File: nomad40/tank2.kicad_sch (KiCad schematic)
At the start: 56 parts

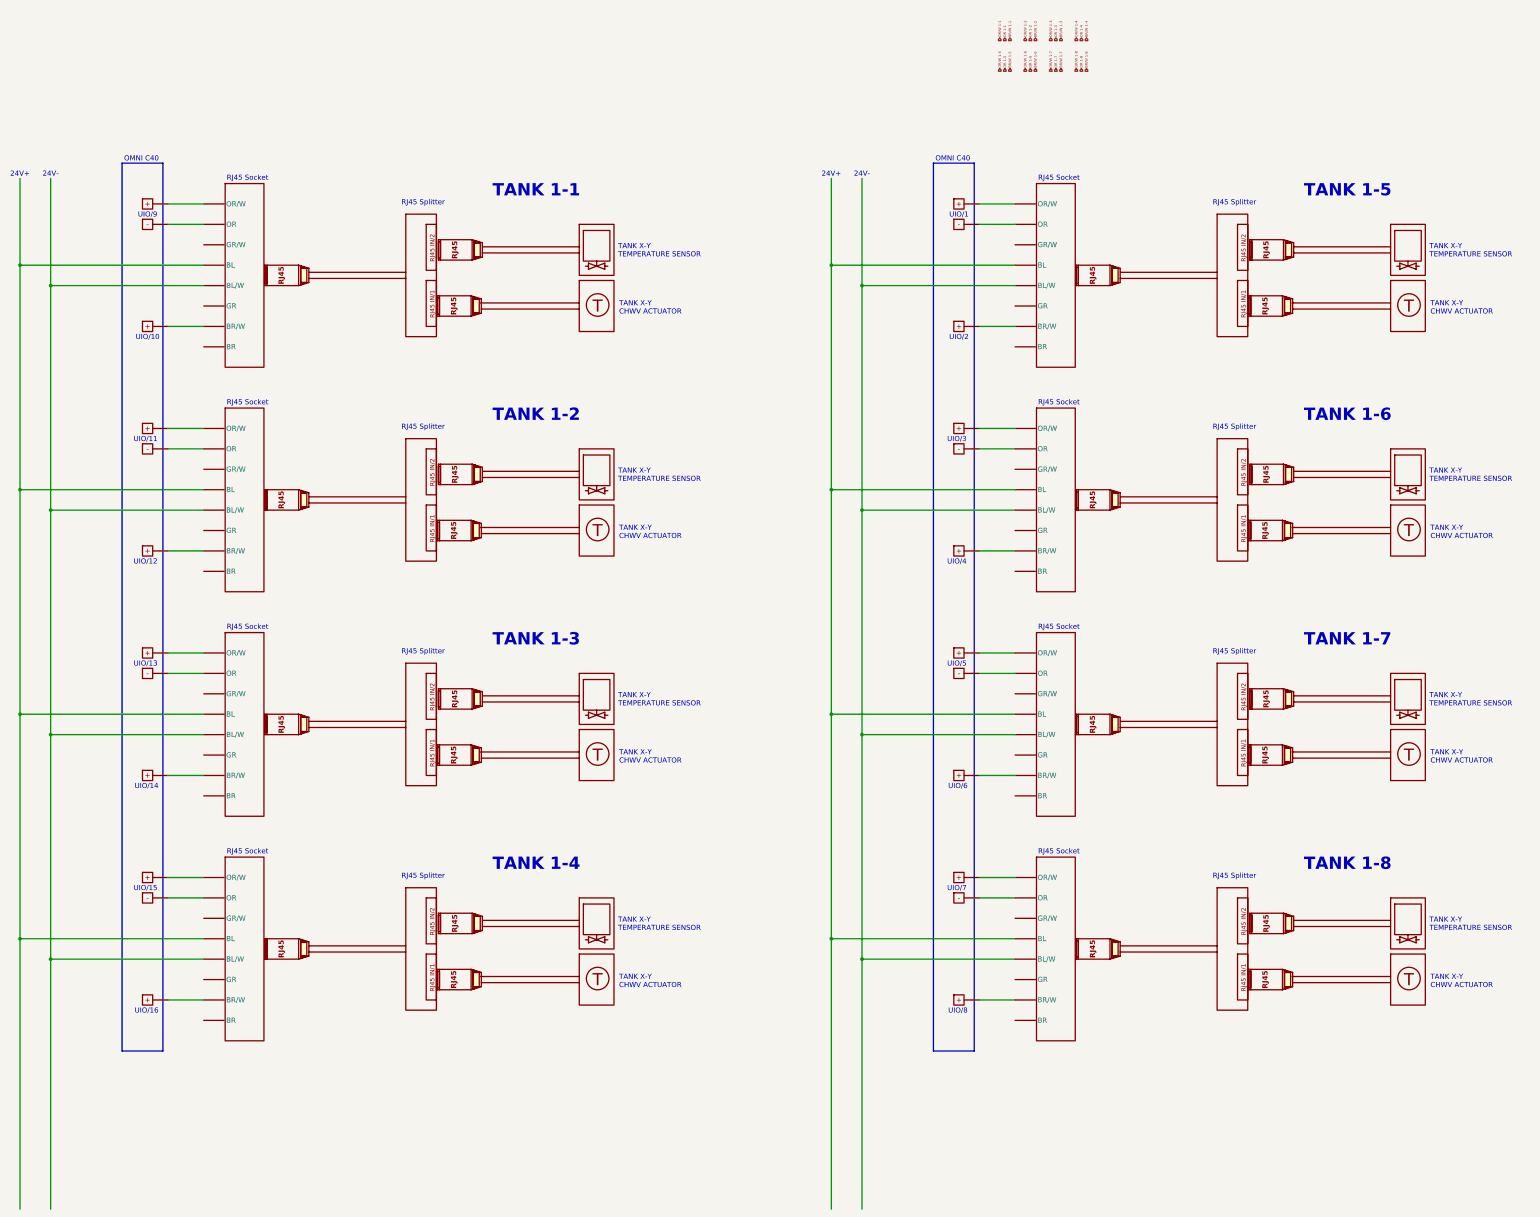
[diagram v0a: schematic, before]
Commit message: add tank2-[1-8] sheet
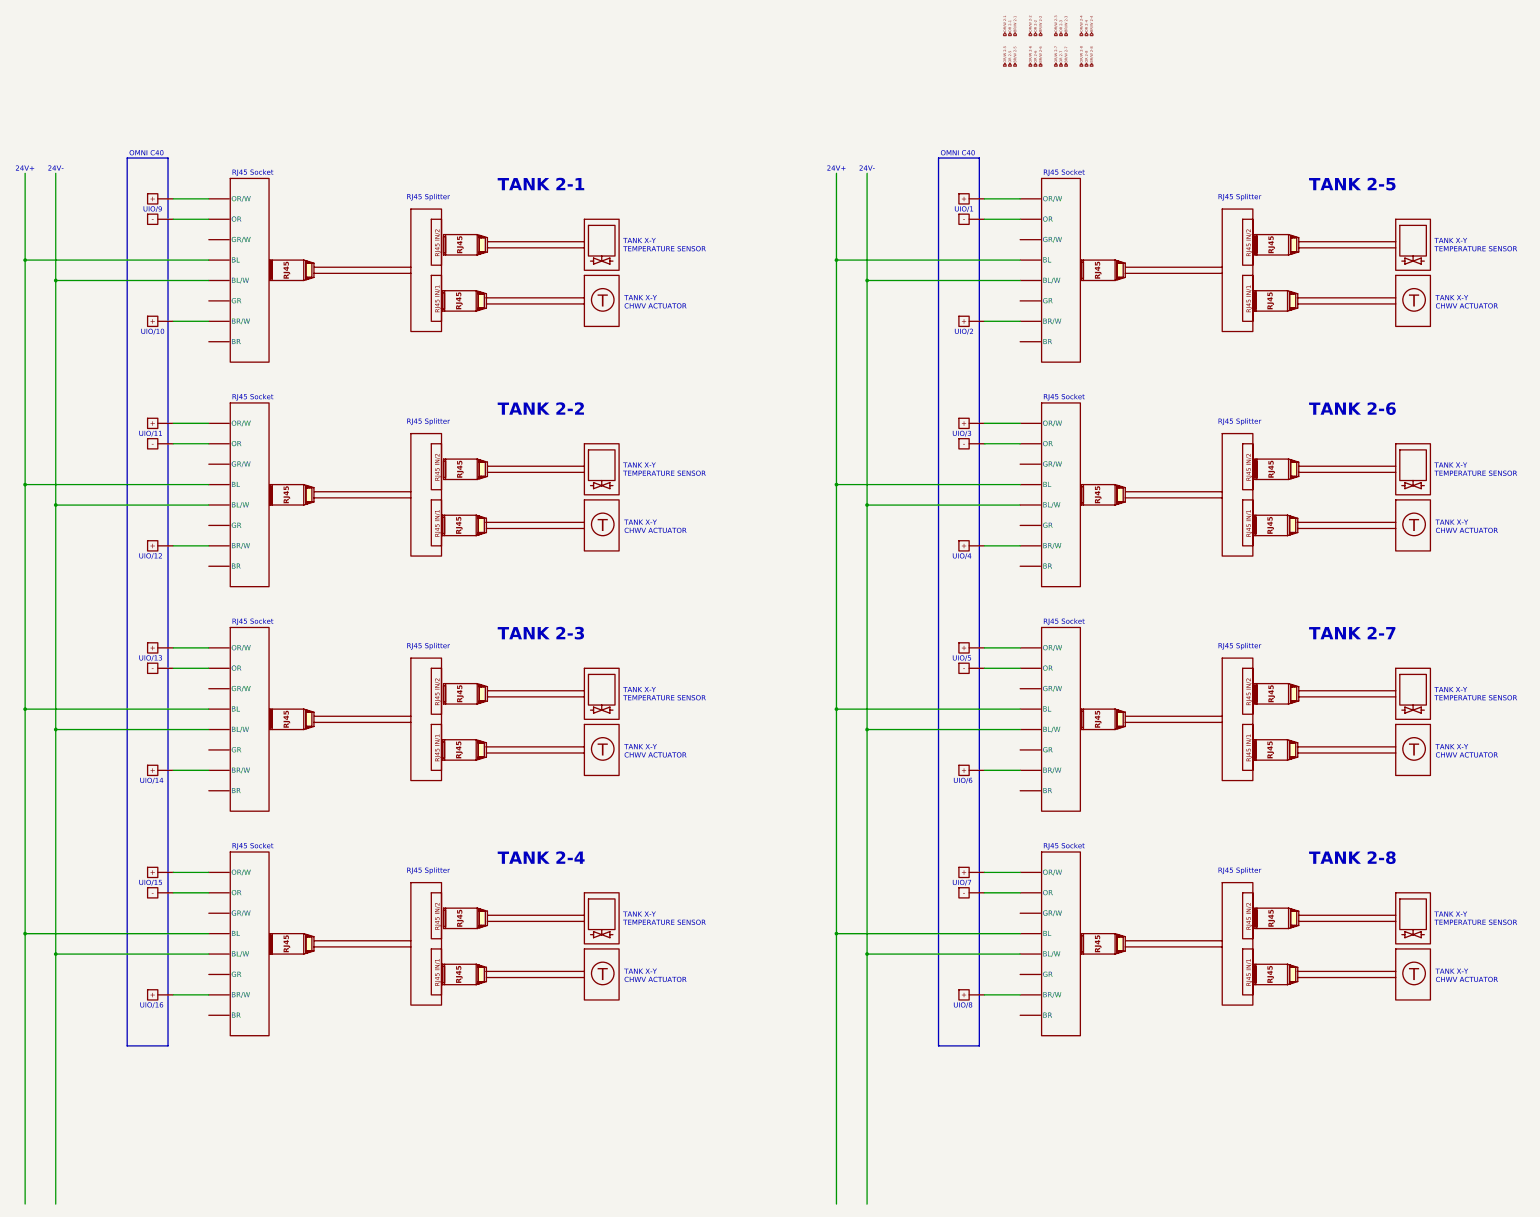
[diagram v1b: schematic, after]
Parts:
- removed U1, U13, U15, U58, U60, U62, U64, U7: (no value), symbol Innotech:Chilled_Water_Valve
- removed U10, U4, U5, U50, U51, U52, U53, U9: (no value), symbol Innotech:RJ45_Socket
- removed U11, U12, U3, U54, U55, U56, U57, U6: (no value), symbol Innotech:RJ45_Breakout
- removed U14, U16, U2, U59, U61, U63, U65, U8: (no value), symbol Innotech:Temperature_Sensor
- removed U18, U20, U22, U24, U26, U28, U30, U32, U34, U36, U38, U40, U42, U44, U46, U48: (no value), symbol Innotech:C40_+terminal
- removed U19, U23, U27, U31, U35, U39, U43, U47: (no value), symbol Innotech:C40_-terminal
- added U100, U101, U74, U75, U76, U77, U98, U99: (no value), symbol Innotech:RJ45_Socket
- added U102, U103, U104, U105, U78, U79, U80, U81: (no value), symbol Innotech:RJ45_Breakout
- added U106, U108, U110, U112, U82, U84, U86, U88: (no value), symbol Innotech:Chilled_Water_Valve
- added U107, U109, U111, U113, U83, U85, U87, U89: (no value), symbol Innotech:Temperature_Sensor
- added U21, U29, U33, U37, U45, U49, U67, U68, U70, U71, U73, U91, U92, U94, U95, U97: (no value), symbol Innotech:C40_+terminal
- added U25, U41, U66, U69, U72, U90, U93, U96: (no value), symbol Innotech:C40_-terminal
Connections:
- new net: U100. (BR), U101. (BR), U98. (BR), U99. (BR) (x2)
- new net: U100. (BR), U94.
- new net: U100. (BR), U92.
- new net: U100. (BR), U93.
- new net: U90., U99. (BR)
- new net: U71., U77. (BR)
- new net: U25., U98. (BR)
- new net: U41., U74. (BR)
- new net: U74. (BR), U75. (BR), U76. (BR), U77. (BR) (x2)
- new net: U45., U74. (BR)
- new net: U37., U74. (BR)
- new net: U73., U77. (BR)
- new net: U72., U77. (BR)
- new net: U29., U98. (BR)
- new net: U21., U98. (BR)
- new net: U91., U99. (BR)
- new net: U33., U99. (BR)
- new net: U68., U76. (BR)
- new net: U101. (BR), U95.
- new net: U69., U76. (BR)
- new net: U101. (BR), U96.
- new net: U101. (BR), U97.
- new net: U49., U75. (BR)
- new net: U66., U75. (BR)
- new net: U67., U75. (BR)
- new net: U70., U76. (BR)
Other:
- note added: "TANK 2-1"
- note added: "TANK 2-2"
- note added: "TANK 2-3"
- note added: "TANK 2-4"
- note added: "TANK 2-5"
- note added: "TANK 2-6"
- note added: "TANK 2-7"
- note added: "TANK 2-8"
- note removed: "TANK 1-1"
- note removed: "TANK 1-2"
- note removed: "TANK 1-3"
- note removed: "TANK 1-4"
- note removed: "TANK 1-5"
- note removed: "TANK 1-6"
- note removed: "TANK 1-7"
- note removed: "TANK 1-8"
